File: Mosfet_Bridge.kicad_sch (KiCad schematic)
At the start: 15 parts

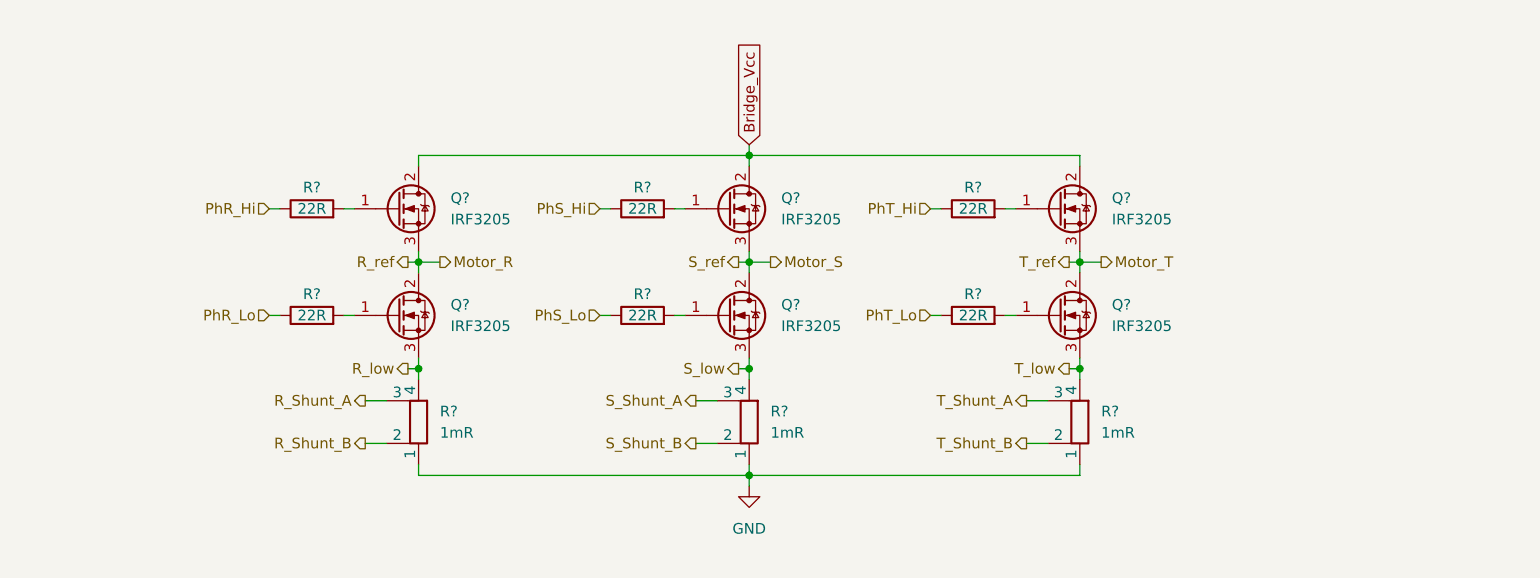
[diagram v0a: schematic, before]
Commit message: Finished basic schematic.
Need to add inline opamps and footprints to all components.
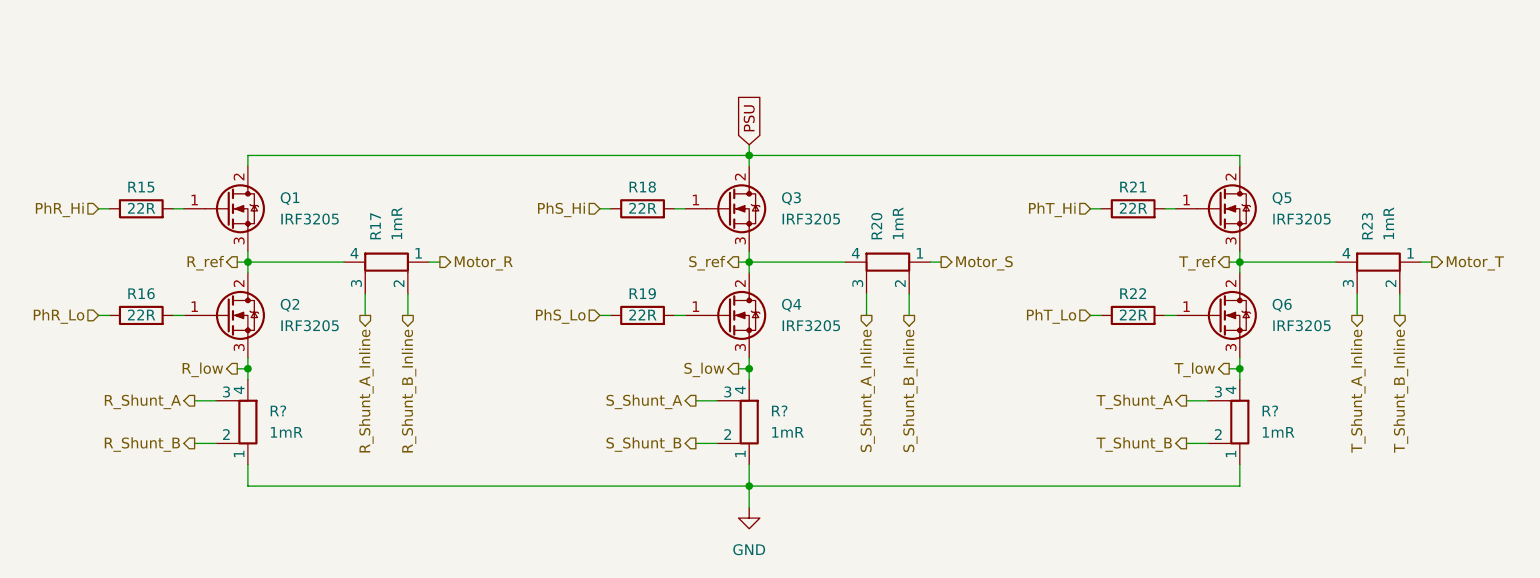
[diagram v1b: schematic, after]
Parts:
- added R? (x3): 1mR, symbol Device:R_Shunt
- R15, R16, R18, R19, R21, R22: renamed from R?; footprint (none) -> Resistor_THT:R_Axial_DIN0207_L6.3mm_D2.5mm_P7.62mm_Horizontal
- gave numbers to parts that had none: 9
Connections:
- net GND: now also R?.1, R?.1, R?.1; no longer R17.1, R20.1, R23.1
- net Motor_R: now also R17.1; no longer Q1.3 (S), Q2.2 (D)
- net Motor_S: now also R20.1; no longer Q3.3 (S), Q4.2 (D)
- net Motor_T: now also R23.1; no longer Q5.3 (S), Q6.2 (D)
- net R_Shunt_A: now also R?.3; no longer R17.3
- net R_Shunt_B: now also R?.2; no longer R17.2
- net R_low: now also R?.4; no longer R17.4
- net S_Shunt_A: now also R?.3; no longer R20.3
- net S_Shunt_B: now also R?.2; no longer R20.2
- net S_low: now also R?.4; no longer R20.4
- net T_Shunt_A: now also R?.3; no longer R23.3
- net T_Shunt_B: now also R?.2; no longer R23.2
- net T_low: now also R?.4; no longer R23.4
- net Bridge_Vcc renamed PSU
- new net R_Shunt_A_Inline: R17.3
- new net R_Shunt_B_Inline: R17.2
- new net R_ref: Q1.3 (S), Q2.2 (D), R17.4
- new net S_Shunt_A_Inline: R20.3
- new net S_Shunt_B_Inline: R20.2
- new net S_ref: Q3.3 (S), Q4.2 (D), R20.4
- new net T_Shunt_A_Inline: R23.3
- new net T_Shunt_B_Inline: R23.2
- new net T_ref: Q5.3 (S), Q6.2 (D), R23.4
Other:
- moved on the sheet: Q1, Q2, Q5, Q6, R15, R16, R17, R20, R21, R22, R23
